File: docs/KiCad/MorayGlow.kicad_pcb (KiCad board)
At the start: 2 copper layers, 46.4 x 38.8 mm, 26 parts, among them J2 RGB LED, J5 Barrel Jack, Q1 IRLML6344TRPBF, Q2 IRLML6344TRPBF, Q3 IRLML6344TRPBF, SW1 SW_DIP_x01, U1 XIAO-ESP32-S3-Plus-SMD

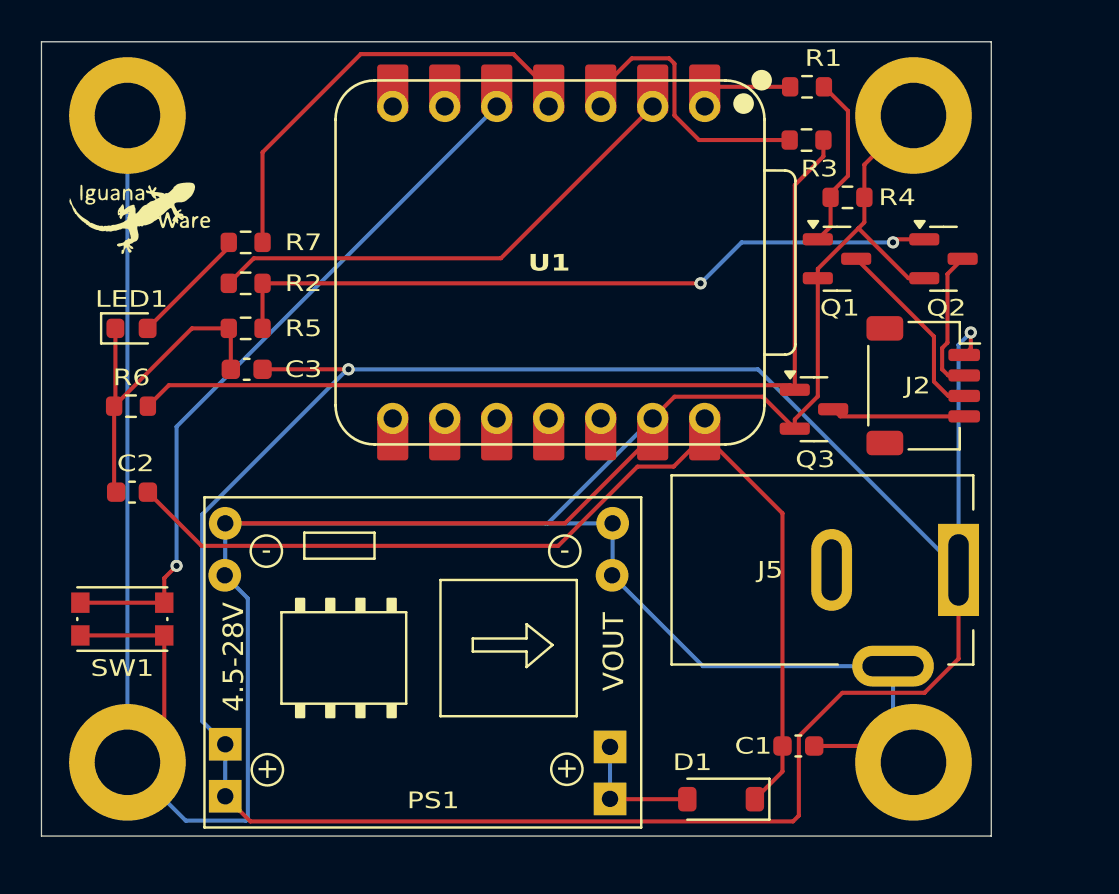
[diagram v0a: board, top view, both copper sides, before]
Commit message: Add enclosure model, update KiCad PCB and project files
- Enclosure/MorrayGlow encosure.3mf — 3D printable enclosure model
- docs/KiCad/MorayGlow.kicad_pcb — PCB layout updates
- docs/KiCad/MorayGlow.kicad_prl — project local settings update
- docs/KiCad/fp-info-cache — footprint cache refresh
- Remove stale KiCad schematic lock file

Co-Authored-By: Claude Sonnet 4.6 <noreply@anthropic.com>
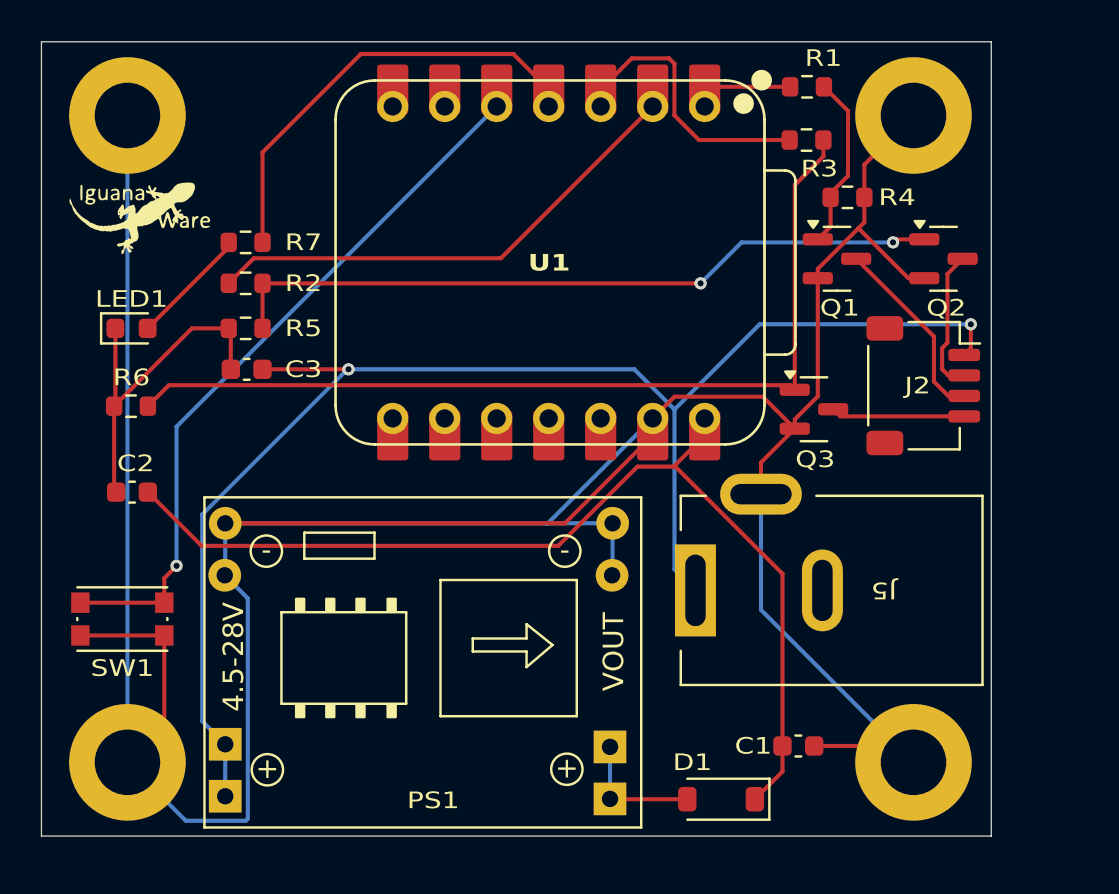
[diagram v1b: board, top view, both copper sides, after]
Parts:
- moved J5 12.9 mm to (173.9, 114.2), turned to 180 degrees
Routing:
- net VCC_12V: track 121.7 -> 72.4 mm
- net Net-(D1-K): track 50.4 -> 49.6 mm
- net <NO NET>: track 189.5 -> 188.9 mm

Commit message: Apply schematic review changes: GPIO fix, component updates, new KiCad files
- Fix critical bug: PIN_BLUE moved from GPIO3 to GPIO6 (D5) — GPIO3 is an
  ESP32-S3 strapping pin that could cause boot issues
- R4/R5/R6 gate pull-downs changed 10kΩ → 100kΩ (saves ~1mA, adequate for
  IRLML6344 gate leakage)
- C3 moved from VCC_12V input to VDD_5V output of MP1584 (correct placement)
- C4 100µF added on VCC_12V at J2 to absorb PWM switching transients
- Update KiCad schematic, PCB, and project files with all reviewed changes
- Update docs/Hardware/BOM.csv, circuit_reference.txt, and docs/index.html
- Remove stale fabrication-toolkit production outputs (can be regenerated)
- Add KiCad .lck files to .gitignore

Co-Authored-By: Claude Sonnet 4.6 <noreply@anthropic.com>
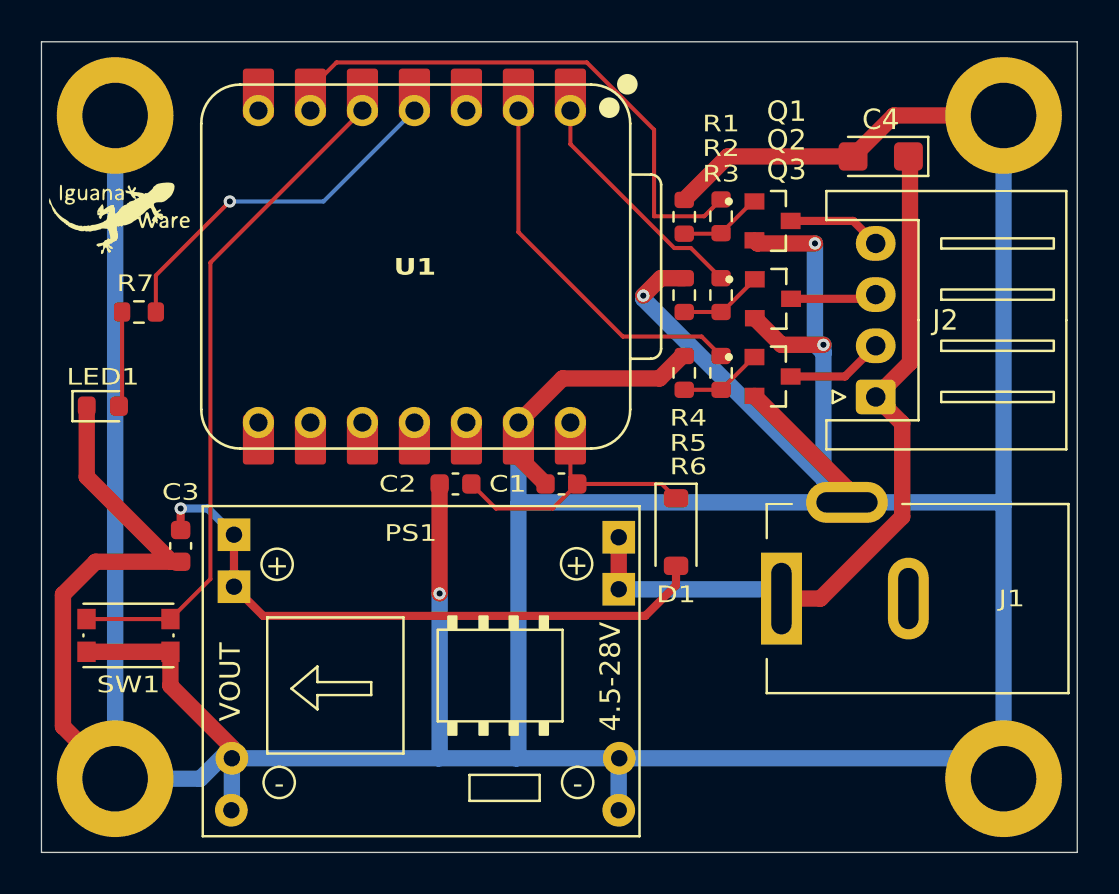
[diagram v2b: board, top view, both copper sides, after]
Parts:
- added C4: 100uF, Capacitor_Tantalum_SMD:CP_EIA-3216-18_Kemet-A, F.Cu at (183.0, 93.0)
- J2: footprint Connector_JST:JST_SH_SM04B-SRSS-TB_1x04-1MP_P1.00mm_Horizontal -> Connector_JST:JST_XH_S4B-XH-A_1x04_P2.50mm_Horizontal
- Q1, Q2, Q3: footprint Package_TO_SOT_SMD:SOT-23 -> IRLML6344TRPBF:TRANS_IRLML6344TRPBF
- R4: renamed from R6; value 10k -> 100k
- R5: renamed from R4; value 10k -> 100k
- R6: renamed from R5; value 10k -> 100k
- moved R4 28.6 mm to (173.4, 96.0), turned to 90 degrees
- moved R3 23.6 mm to (175.2, 103.6), turned to 90 degrees
- moved R6 21.5 mm to (173.4, 103.6), turned to 90 degrees
- moved C1 17.3 mm to (167.4, 109.0), turned to 180 degrees
- moved C2 15.8 mm to (162.2, 109.0)
- moved D1 13.2 mm to (173.0, 111.3), turned to -90 degrees
- moved R2 11.0 mm to (175.2, 99.8), turned to 90 degrees
- moved R5 9.30 mm to (173.4, 99.8), turned to 90 degrees
- moved C3 9.21 mm to (148.8, 112.0), turned to 90 degrees
- moved Q2 8.55 mm to (177.7, 100.0)
- moved G*** 7.73 mm to (167.8, 99.2)
- moved U1 6.56 mm to (160.2, 98.4)
- moved R7 6.22 mm to (146.8, 100.6)
- moved R1 5.60 mm to (175.2, 95.9), turned to 90 degrees
- moved H4 4.47 mm to (189.0, 123.4)
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- renumbered J5 to J1, R3 to R1, R1 to R2, R2 to R3
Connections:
- C1 pad 2: <NO NET> -> GND
- C2 pad 2: <NO NET> -> GND
- C3 pad 1: VCC_12V -> GND
- C3 pad 2: <NO NET> -> VDD_5V
- H1 pad 1: <NO NET> -> GND
- H2 pad 1: <NO NET> -> GND
- H3 pad 1: <NO NET> -> GND
- H4 pad 1: <NO NET> -> GND
- J1 pad 3: <NO NET> -> GND
- LED1 pad 1: <NO NET> -> GND
- PS1 pad 2: <NO NET> -> GND
- PS1 pad 4: <NO NET> -> GND
- Q1 pad 2: <NO NET> -> GND
- Q1 pad 3: LED_R -> LED_B
- Q2 pad 2: <NO NET> -> GND
- Q2 pad 3: LED_G -> LED_R
- Q3 pad 2: <NO NET> -> GND
- Q3 pad 3: LED_B -> LED_G
- R1 pad 1: Net-(Q3-Pad1) -> Net-(Q1-Pad1)
- R2 pad 1: Net-(Q1-Pad1) -> Net-(Q2-Pad1)
- R3 pad 1: Net-(Q2-Pad1) -> Net-(Q3-Pad1)
- R4 pad 1: Net-(Q3-Pad1) -> Net-(Q1-Pad1)
- R4 pad 2: <NO NET> -> GND
- R5 pad 1: Net-(Q1-Pad1) -> Net-(Q2-Pad1)
- R5 pad 2: <NO NET> -> GND
- R6 pad 1: Net-(Q2-Pad1) -> Net-(Q3-Pad1)
- R6 pad 2: <NO NET> -> GND
- SW1 pad 2: <NO NET> -> GND
- U1 pad 13: <NO NET> -> GND
- U1 pad 3: RGB_B -> unconnected-(U1-GPIO3_A2_D2-Pad3)
- U1 pad 6: unconnected-(U1-GPIO6_A5_D5_SCL-Pad6) -> RGB_B
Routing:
- net GND: track 0.00 -> 279.1 mm, vias 0 -> 4
- net <NO NET>: track 188.9 -> 0.00 mm
- net Net-(Q3-Pad1): track 44.9 -> 4.06 mm
- net VCC_12V: track 72.4 -> 36.3 mm, vias 2 -> 0
- net Net-(D1-K): track 49.6 -> 13.6 mm
- net Net-(Q2-Pad1): track 35.4 -> 4.06 mm, vias 2 -> 0
- net VDD_5V: track 6.32 -> 30.5 mm, vias 0 -> 1
- net RGB_B: track 13.0 -> 26.5 mm
- net RGB_R: track 4.23 -> 11.7 mm
- net RGB_G: track 24.3 -> 18.3 mm
- net LED_R: track 9.34 -> 3.93 mm
- net Net-(Q1-Pad1): track 8.55 -> 3.97 mm
- net STATUS_LED: track 21.1 -> 17.8 mm, vias 0 -> 1
- net CMD_BTN: track 35.1 -> 32.8 mm, vias 1 -> 0
- net LED_G: track 7.01 -> 4.78 mm
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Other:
- board size 46.4 x 38.8 mm -> 50.6 x 39.6 mm
